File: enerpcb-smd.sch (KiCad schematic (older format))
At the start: 22 parts, among them K1 VS1, K2 VS2, K3 CONN_1, K4 CONN_1, P2 IO1, P3 IO2, P4 PROGRAM, P5 V1, P6 V2, P7 GND1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

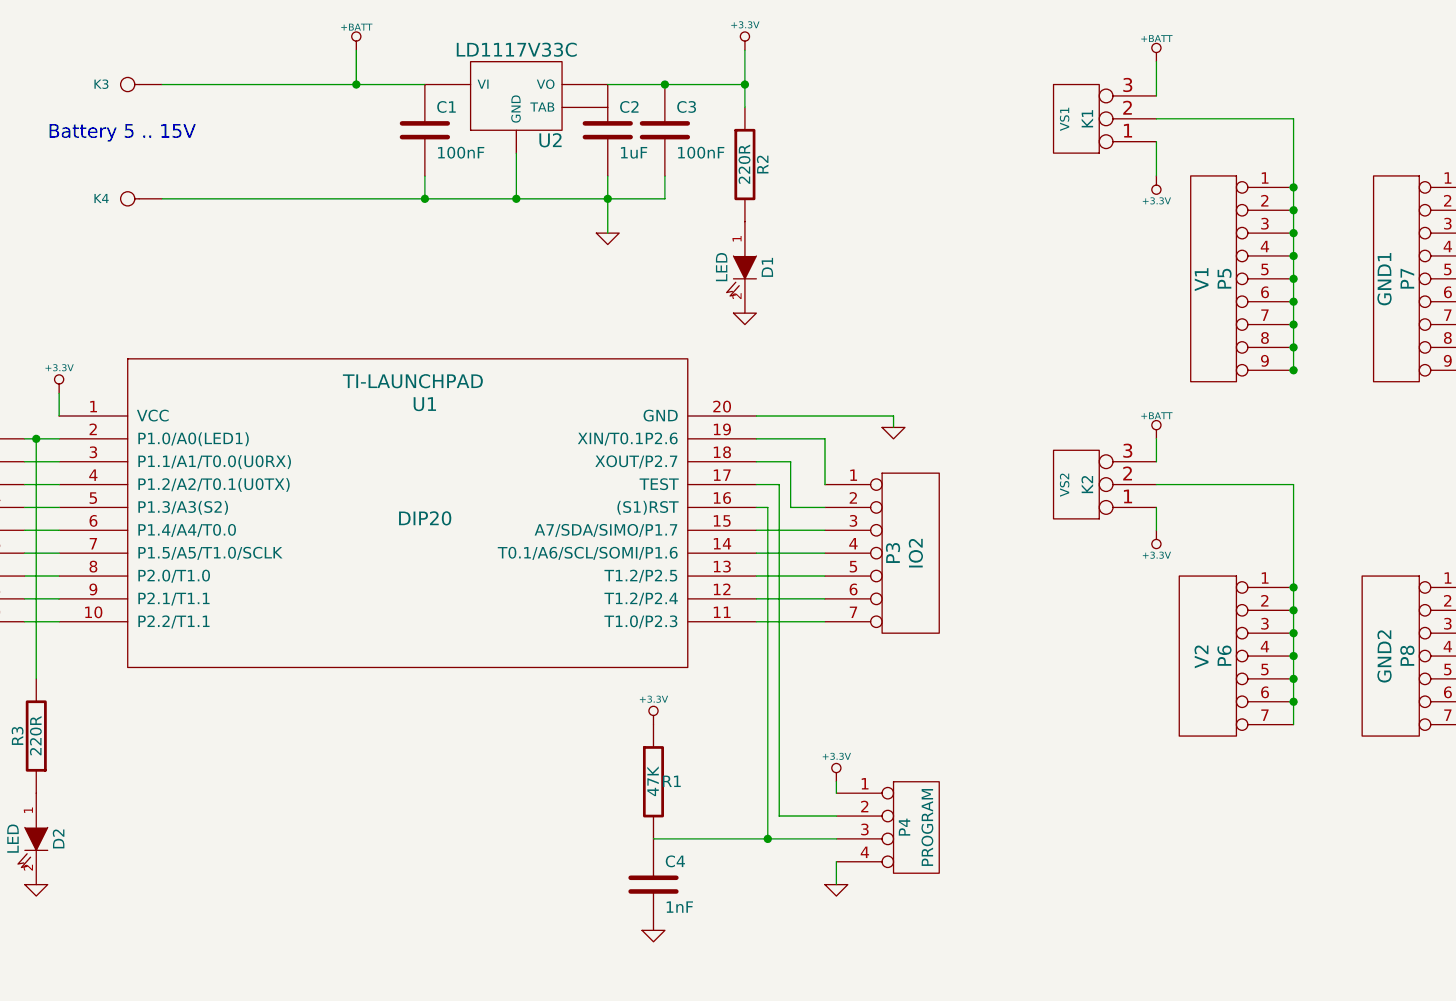
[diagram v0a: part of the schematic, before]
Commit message: Routed SMD version: OK
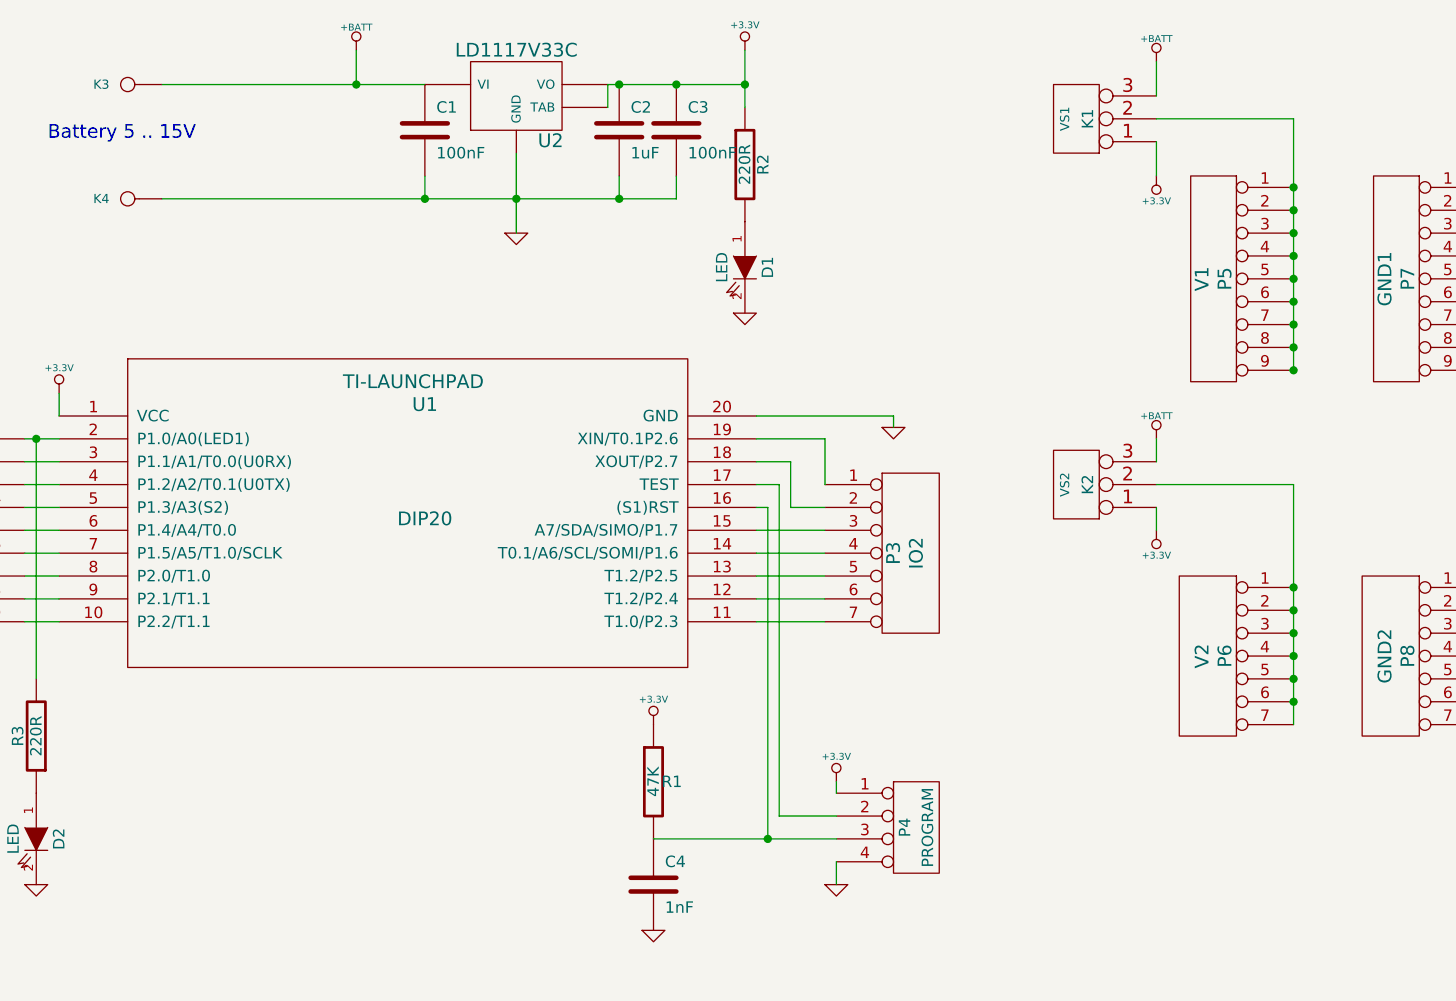
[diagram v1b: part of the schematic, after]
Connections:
- net +3.3V: now also U2.4 (TAB)
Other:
- moved on the sheet: C2, C3
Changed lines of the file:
@@
-EESchema Schematic File Version 2  date 1/1/2013 8:38:13 PM
+EESchema Schematic File Version 2  date 1/5/2013 4:17:03 PM
 LIBS:power
 LIBS:device
@@
 LIBS:valves
 LIBS:ti-launchpad
-LIBS:enerpcb-cache
+LIBS:enerpcb-smd-cache
 EELAYER 25  0
 EELAYER END
@@
 Sheet 1 1
 Title ""
-Date "1 jan 2013"
+Date "5 jan 2013"
 Rev ""
 Comp ""
@@
 $EndDescr
 Wire Wire Line
-	7000 2250 7000 1150
-Wire Wire Line
-	5250 2500 5250 2450
-Wire Wire Line
-	5250 2450 4650 2450
-Wire Wire Line
-	4950 2750 4950 2550
-Wire Wire Line
-	4950 2550 4650 2550
-Wire Wire Line
-	4650 2750 4750 2750
+	2050 1500 4300 1500
+Wire Wire Line
+	4600 1000 4000 1000
+Wire Wire Line
+	4000 1000 4000 1100
+Wire Wire Line
+	4800 2850 4800 2650
+Wire Wire Line
+	4800 2850 4950 2850
+Wire Wire Line
+	4650 2850 4700 2850
+Wire Wire Line
+	4950 2950 4650 2950
+Wire Wire Line
+	4950 3150 4650 3150
+Wire Wire Line
+	4950 3350 4650 3350
+Wire Wire Line
+	4750 4200 4750 2750
+Connection ~ 1500 2550
+Wire Wire Line
+	1500 2550 1500 3600
+Wire Wire Line
+	1450 3250 1600 3250
+Wire Wire Line
+	1450 3050 1600 3050
+Wire Wire Line
+	1450 2850 1600 2850
+Wire Wire Line
+	1450 2650 1600 2650
+Wire Wire Line
+	5000 4300 4200 4300
+Wire Wire Line
+	5000 4400 5000 4500
+Connection ~ 4600 1000
+Wire Wire Line
+	4600 850  4600 1100
+Wire Wire Line
+	2050 1000 3200 1000
+Connection ~ 3200 1500
+Wire Wire Line
+	3200 1500 3200 1400
+Wire Wire Line
+	7800 1450 7800 4000
+Wire Wire Line
+	7000 3800 7000 2750
+Wire Wire Line
+	7000 2750 6400 2750
+Wire Wire Line
+	6400 2550 6400 2650
+Connection ~ 7800 3800
+Connection ~ 7800 3600
+Connection ~ 7800 3400
+Connection ~ 7800 3300
+Connection ~ 7800 2250
+Connection ~ 7800 2050
+Connection ~ 7800 1950
+Connection ~ 7800 1750
+Connection ~ 7800 1550
+Connection ~ 7000 3700
+Connection ~ 7000 3500
+Connection ~ 7000 3200
+Connection ~ 7000 2150
+Connection ~ 7000 1950
+Connection ~ 7000 1750
+Connection ~ 7000 1550
+Wire Wire Line
+	6400 1150 7000 1150
+Wire Wire Line
+	6400 900  6400 1050
+Wire Wire Line
+	1600 2350 1600 2450
+Wire Wire Line
+	2900 850  2900 1000
+Connection ~ 2900 1000
+Wire Wire Line
+	6400 1400 6400 1250
+Connection ~ 7000 1450
+Connection ~ 7000 1650
+Connection ~ 7000 1850
+Connection ~ 7000 2050
+Connection ~ 7000 2250
+Connection ~ 7000 3400
+Connection ~ 7000 3300
+Connection ~ 7000 3600
+Connection ~ 7800 1650
+Connection ~ 7800 1850
+Connection ~ 7800 2150
+Connection ~ 7800 3200
+Connection ~ 7800 3500
+Connection ~ 7800 3700
+Wire Wire Line
+	6400 2850 6400 2950
+Connection ~ 3600 1500
+Wire Wire Line
+	4300 1500 4300 1400
+Connection ~ 4300 1000
+Wire Wire Line
+	5000 4100 5000 4050
+Wire Wire Line
+	1450 2550 1600 2550
+Wire Wire Line
+	1450 2750 1600 2750
+Wire Wire Line
+	1450 2950 1600 2950
+Wire Wire Line
+	1450 3150 1600 3150
+Wire Wire Line
+	1450 3350 1600 3350
+Wire Wire Line
+	4800 2650 4650 2650
+Wire Wire Line
+	4750 4200 5000 4200
+Wire Wire Line
+	4700 2850 4700 4300
+Connection ~ 4700 4300
+Wire Wire Line
+	4950 3250 4650 3250
 Wire Wire Line
 	4950 3050 4650 3050
 Wire Wire Line
-	4950 3250 4650 3250
-Connection ~ 4700 4300
-Wire Wire Line
-	4700 4300 4700 2850
-Wire Wire Line
-	5000 4200 4750 4200
-Wire Wire Line
-	4650 2650 4800 2650
-Wire Wire Line
-	1450 3350 1600 3350
-Wire Wire Line
-	1450 3150 1600 3150
-Wire Wire Line
-	1450 2950 1600 2950
-Wire Wire Line
-	1450 2750 1600 2750
-Wire Wire Line
-	1450 2550 1600 2550
-Wire Wire Line
-	5000 4100 5000 4050
-Connection ~ 4250 1000
-Wire Wire Line
-	4250 1400 4250 1500
-Wire Wire Line
-	4250 1500 2050 1500
-Connection ~ 3600 1500
-Wire Wire Line
-	3600 1500 3600 1300
-Wire Wire Line
-	6400 2850 6400 2950
-Connection ~ 7800 3700
-Connection ~ 7800 3500
-Connection ~ 7800 3200
-Connection ~ 7800 2150
-Connection ~ 7800 1850
-Connection ~ 7800 1650
-Connection ~ 7000 3600
-Connection ~ 7000 3300
-Connection ~ 7000 3400
-Connection ~ 7000 2250
-Connection ~ 7000 2050
-Connection ~ 7000 1850
-Connection ~ 7000 1650
-Connection ~ 7000 1450
-Wire Wire Line
-	6400 1400 6400 1250
-Connection ~ 2900 1000
-Wire Wire Line
-	2900 850  2900 1000
-Wire Wire Line
-	1600 2350 1600 2450
-Wire Wire Line
-	6400 900  6400 1050
-Wire Wire Line
-	7000 1150 6400 1150
-Connection ~ 7000 1550
-Connection ~ 7000 1750
-Connection ~ 7000 1950
-Connection ~ 7000 2150
-Connection ~ 7000 3200
-Connection ~ 7000 3500
-Connection ~ 7000 3700
-Connection ~ 7800 1550
-Connection ~ 7800 1750
-Connection ~ 7800 1950
-Connection ~ 7800 2050
-Connection ~ 7800 2250
-Connection ~ 7800 3300
-Connection ~ 7800 3400
-Connection ~ 7800 3600
-Connection ~ 7800 3800
-Wire Wire Line
-	6400 2550 6400 2650
-Wire Wire Line
-	6400 2750 7000 2750
-Wire Wire Line
-	7000 2750 7000 3800
-Wire Wire Line
-	7800 1450 7800 4000
-Wire Wire Line
-	3200 1500 3200 1400
-Connection ~ 3200 1500
-Connection ~ 4000 1500
-Wire Wire Line
-	4000 1650 4000 1400
-Wire Wire Line
-	2050 1000 3200 1000
-Wire Wire Line
-	4600 1000 4000 1000
-Wire Wire Line
-	4600 850  4600 1100
-Connection ~ 4600 1000
-Wire Wire Line
-	5000 4400 5000 4500
-Wire Wire Line
-	5000 4300 4200 4300
-Wire Wire Line
-	1450 2650 1600 2650
-Wire Wire Line
-	1450 2850 1600 2850
-Wire Wire Line
-	1450 3050 1600 3050
-Wire Wire Line
-	1450 3250 1600 3250
-Wire Wire Line
-	1500 2550 1500 3600
-Connection ~ 1500 2550
-Wire Wire Line
-	4750 4200 4750 2750
-Wire Wire Line
-	4950 3350 4650 3350
-Wire Wire Line
-	4950 3150 4650 3150
-Wire Wire Line
-	4950 2950 4650 2950
-Wire Wire Line
-	4700 2850 4650 2850
-Wire Wire Line
-	4950 2850 4800 2850
-Wire Wire Line
-	4800 2850 4800 2650
+	4750 2750 4650 2750
+Wire Wire Line
+	4650 2550 4950 2550
+Wire Wire Line
+	4950 2550 4950 2750
+Wire Wire Line
+	4650 2450 5250 2450
+Wire Wire Line
+	5250 2450 5250 2500
+Wire Wire Line
+	7000 1150 7000 2250
+Wire Wire Line
+	3600 1650 3600 1300
+Connection ~ 4050 1000
+Wire Wire Line
+	4050 1400 4050 1500
+Connection ~ 4050 1500
+$Comp
+L LD1117V33C U2
+U 1 1 50E2C9E5
+P 3600 1050
+F 0 "U2" H 3750 854 60  0000 C CNN
+F 1 "LD1117V33C" H 3600 1250 60  0000 C CNN
+	1    3600 1050
+	1    0    0    -1
+$EndComp
 Text Notes 1550 1250 0    60   ~ 0
 Battery 5 .. 15V
@@
 $EndComp
 $Comp
-L LD1117V33C U2
-U 1 1 50E2C9E5
-P 3600 1050
-F 0 "U2" H 3750 854 60  0000 C CNN
-F 1 "LD1117V33C" H 3600 1250 60  0000 C CNN
-	1    3600 1050
-	1    0    0    -1
-$EndComp
-$Comp
 L GND #PWR02
 U 1 1 50E2C789
@@
 L C C3
 U 1 1 50E2C4B7
-P 4250 1200
-F 0 "C3" H 4300 1300 50  0000 L CNN
-F 1 "100nF" H 4300 1100 50  0000 L CNN
-	1    4250 1200
+P 4300 1200
+F 0 "C3" H 4350 1300 50  0000 L CNN
+F 1 "100nF" H 4350 1100 50  0000 L CNN
+	1    4300 1200
 	1    0    0    -1
 $EndComp
@@
 L GND #PWR04
 U 1 1 50E1B581
-P 4000 1650
-F 0 "#PWR04" H 4000 1650 30  0001 C CNN
-F 1 "GND" H 4000 1580 30  0001 C CNN
-	1    4000 1650
+P 3600 1650
+F 0 "#PWR04" H 3600 1650 30  0001 C CNN
+F 1 "GND" H 3600 1580 30  0001 C CNN
+	1    3600 1650
 	1    0    0    -1
 $EndComp
@@
 L C C2
 U 1 1 50E1969F
-P 4000 1200
-F 0 "C2" H 4050 1300 50  0000 L CNN
-F 1 "1uF" H 4050 1100 50  0000 L CNN
-	1    4000 1200
-	1    0    0    -1
-$EndComp
+P 4050 1200
+F 0 "C2" H 4100 1300 50  0000 L CNN
+F 1 "1uF" H 4100 1100 50  0000 L CNN
+	1    4050 1200
+	1    0    0    -1
+$EndComp

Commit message: As ordered
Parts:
- C1, C3: Farnell (none) -> 1856307; PRICE (none) -> 0.06
- C2: Farnell (none) -> 1856632; PRICE (none) -> 0.06
- C4: Farnell (none) -> 1856408; PRICE (none) -> 0.06
- D1: value LED -> LED-R; footprint (none) -> LED0603; Farnell (none) -> 8554641; MFG (none) -> HSMH-C190; PRICE (none) -> 0.06
- D2: value LED -> LED-G; footprint (none) -> LED0603; Farnell (none) -> 1226372; MFG (none) -> LGQ971; PRICE (none) -> 0.07
- P2: Farnell (none) -> 2035689; MFG (none) -> SAMTEC TSW-109-07-T-S; PRICE (none) -> 0.85
- P3: Farnell (none) -> 1924186; MFG (none) -> FCI 68000-107HLF; PRICE (none) -> 0.42
- P4: footprint (none) -> SIL-4; Farnell (none) -> 1756958; MFG (none) -> MOLEX 90120-0124 HEADER, 2.54MM, 4WAY; PRICE (none) -> 0.15
- P5, P7: Farnell (none) -> 2035689; PRICE (none) -> 0.85
- P6, P8: Farnell (none) -> 1924186; PRICE (none) -> 0.42
- R1: Farnell (none) -> 2074475; PRICE (none) -> 0.03
- R2, R3: Farnell (none) -> 9233920; PRICE (none) -> 0.03
- U1: value TI-LAUNCHPAD -> MSP430G2212IPW20; footprint DIP20 -> TSSOP20; Farnell (none) -> 1866866; MFG (none) -> TI MSP430G2212IPW20 2kB FLASH 256b RAM; PRICE (none) -> 0.7
- U2: Farnell (none) -> 1467776; PRICE (none) -> 1
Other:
- note added: "MSP430G2212IPW20: FARNELL# 1866866 (2kB 256b 1xTA3 8xCMP), E0.70@1, E0.56@100"
- note added: "MSP430G2302IPW20: FARNELL# 1866883 (4kB 256b 1xTA3 8xCMP), E1.6@1, E0.68@100"
- note added: "MSP430G2352IPW20: FARNELL# 1866896 (4kB 256b 1xTA3 8xCMP 8xADC), E0.90@1, E0.69@100"
- note added: "MSP430G2452IPW20R: FARNELL# 1865387 (8kB 256b 1xTA3 8xCMP, 8xADC), E2.48@1, E0.80@100"
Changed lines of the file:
@@
-EESchema Schematic File Version 2  date 1/5/2013 4:17:03 PM
+EESchema Schematic File Version 2  date 1/6/2013 1:15:40 AM
 LIBS:power
 LIBS:device
@@
 Sheet 1 1
 Title ""
-Date "5 jan 2013"
+Date "6 jan 2013"
 Rev ""
 Comp ""
@@
 Comment4 ""
 $EndDescr
+Text Notes 1300 5550 0    100  ~ 0
+MSP430G2452IPW20R: FARNELL#  1865387  (8kB 256b 1xTA3 8xCMP, 8xADC), E2.48@1, E0.80@100
+Text Notes 1300 5150 0    100  ~ 0
+MSP430G2302IPW20: FARNELL#  1866883  (4kB 256b 1xTA3 8xCMP), E1.6@1, E0.68@100
+Text Notes 1300 4950 0    100  ~ 0
+MSP430G2212IPW20: FARNELL#  1866866 (2kB 256b 1xTA3 8xCMP), E0.70@1, E0.56@100
+Text Notes 1300 5350 0    100  ~ 0
+MSP430G2352IPW20: FARNELL#  1866896 (4kB 256b 1xTA3 8xCMP 8xADC), E0.90@1, E0.69@100
 Wire Wire Line
 	2050 1500 4300 1500
@@
 F 0 "U2" H 3750 854 60  0000 C CNN
 F 1 "LD1117V33C" H 3600 1250 60  0000 C CNN
+F 4 "1467776 " H 3600 1050 60  0001 C CNN "Farnell"
+F 5 "1" H 3600 1050 60  0001 C CNN "PRICE"
 	1    3600 1050
 	1    0    0    -1
@@
 P 1500 4300
 F 0 "D2" H 1500 4400 50  0000 C CNN
-F 1 "LED" H 1500 4200 50  0000 C CNN
+F 1 "LED-G" H 1500 4200 50  0000 C CNN
+F 2 "LED0603" H 1500 4300 60  0001 C CNN
+F 4 "1226372 " H 1500 4300 60  0001 C CNN "Farnell"
+F 5 "0.07" H 1500 4300 60  0001 C CNN "PRICE"
+F 6 "LGQ971 " H 1500 4300 60  0001 C CNN "MFG"
 	1    1500 4300
 	0    1    1    0
@@
 F 0 "R3" V 1580 3850 50  0000 C CNN
 F 1 "220R" V 1500 3850 50  0000 C CNN
+F 4 " 9233920" H 1500 3850 60  0001 C CNN "Farnell"
+F 5 "0.03" H 1500 3850 60  0001 C CNN "PRICE"
 	1    1500 3850
 	-1   0    0    1
@@
 F 0 "C3" H 4350 1300 50  0000 L CNN
 F 1 "100nF" H 4350 1100 50  0000 L CNN
+F 4 "1856307" H 4300 1200 60  0001 C CNN "Farnell"
+F 5 "0.06" H 4300 1200 60  0001 C CNN "PRICE"
 	1    4300 1200
 	1    0    0    -1
@@
 F 0 "C4" H 4250 4600 50  0000 L CNN
 F 1 "1nF" H 4250 4400 50  0000 L CNN
+F 4 "1856408" H 4200 4500 60  0001 C CNN "Farnell"
+F 5 "0.06" H 4200 4500 60  0001 C CNN "PRICE"
 	1    4200 4500
 	1    0    0    -1
@@
 F 0 "R2" V 4680 1350 50  0000 C CNN
 F 1 "220R" V 4600 1350 50  0000 C CNN
+F 4 " 9233920" H 4600 1350 60  0001 C CNN "Farnell"
+F 5 "0.03" H 4600 1350 60  0001 C CNN "PRICE"
 	1    4600 1350
 	1    0    0    -1
@@
 P 4600 1800
 F 0 "D1" H 4600 1900 50  0000 C CNN
-F 1 "LED" H 4600 1700 50  0000 C CNN
+F 1 "LED-R" H 4600 1700 50  0000 C CNN
+F 2 "LED0603" H 4600 1800 60  0001 C CNN
+F 4 "8554641" H 4600 1800 60  0001 C CNN "Farnell"
+F 5 "0.06" H 4600 1800 60  0001 C CNN "PRICE"
+F 6 "HSMH-C190" H 4600 1800 60  0001 C CNN "MFG"
 	1    4600 1800
 	0    1    1    0
@@
 F 0 "R1" H 4280 4050 50  0000 C CNN
 F 1 "47K" V 4200 4050 50  0000 C CNN
+F 4 "2074475 " H 4200 4050 60  0001 C CNN "Farnell"
+F 5 "0.03" H 4200 4050 60  0001 C CNN "PRICE"
 	1    4200 4050
 	1    0    0    -1
@@
 F 0 "P8" V 7400 3500 60  0000 C CNN
 F 1 "GND2" V 7500 3500 60  0000 C CNN
+F 4 "1924186" H 7450 3500 60  0001 C CNN "Farnell"
+F 5 "0.42" H 7450 3500 60  0001 C CNN "PRICE"
 	1    7450 3500
 	-1   0    0    -1
@@
 F 0 "P7" V 7400 1850 60  0000 C CNN
 F 1 "GND1" V 7500 1850 60  0000 C CNN
+F 4 "2035689 " H 7450 1850 60  0001 C CNN "Farnell"
+F 5 "0.85" H 7450 1850 60  0001 C CNN "PRICE"
 	1    7450 1850
 	-1   0    0    -1
@@
 F 0 "C2" H 4100 1300 50  0000 L CNN
 F 1 "1uF" H 4100 1100 50  0000 L CNN
+F 4 "1856632 " H 4050 1200 60  0001 C CNN "Farnell"
+F 5 "0.06" H 4050 1200 60  0001 C CNN "PRICE"
 	1    4050 1200
 	1    0    0    -1
@@
 F 0 "C1" H 3250 1300 50  0000 L CNN
 F 1 "100nF" H 3250 1100 50  0000 L CNN
+F 4 "1856307" H 3200 1200 60  0001 C CNN "Farnell"
+F 5 "0.06" H 3200 1200 60  0001 C CNN "PRICE"
 	1    3200 1200
 	1    0    0    -1
@@
 F 0 "P6" V 6600 3500 60  0000 C CNN
 F 1 "V2" V 6700 3500 60  0000 C CNN
+F 4 "1924186" H 6650 3500 60  0001 C CNN "Farnell"
+F 5 "0.42" H 6650 3500 60  0001 C CNN "PRICE"
 	1    6650 3500
 	-1   0    0    -1
@@
 F 0 "P5" V 6600 1850 60  0000 C CNN
 F 1 "V1" V 6700 1850 60  0000 C CNN
+F 4 "2035689 " H 6650 1850 60  0001 C CNN "Farnell"
+F 5 "0.85" H 6650 1850 60  0001 C CNN "PRICE"
 	1    6650 1850
 	-1   0    0    -1
@@
 F 0 "P4" V 5300 4250 50  0000 C CNN
 F 1 "PROGRAM" V 5400 4250 50  0000 C CNN
+F 2 "SIL-4" H 5350 4250 60  0001 C CNN
+F 4 "1756958" H 5350 4250 60  0001 C CNN "Farnell"
+F 5 "0.15" H 5350 4250 60  0001 C CNN "PRICE"
+F 6 "MOLEX 90120-0124  HEADER, 2.54MM, 4WAY" H 5350 4250 60  0001 C CNN "MFG"
 	1    5350 4250
 	1    0    0    -1
@@
 F 0 "P2" V 1050 2950 60  0000 C CNN
 F 1 "IO1" V 1150 2950 60  0000 C CNN
+F 4 "2035689 " H 1100 2950 60  0001 C CNN "Farnell"
+F 5 "0.85" H 1100 2950 60  0001 C CNN "PRICE"
+F 6 "SAMTEC TSW-109-07-T-S " H 1100 2950 60  0001 C CNN "MFG"
 	1    1100 2950
 	-1   0    0    -1
@@
 F 0 "P3" V 5250 3050 60  0000 C CNN
 F 1 "IO2" V 5350 3050 60  0000 C CNN
+F 4 "1924186" H 5300 3050 60  0001 C CNN "Farnell"
+F 5 "0.42" H 5300 3050 60  0001 C CNN "PRICE"
+F 6 "FCI 68000-107HLF " H 5300 3050 60  0001 C CNN "MFG"
 	1    5300 3050
 	1    0    0    -1
@@
 P 3200 2900
 F 0 "U1" H 3200 3400 60  0000 C CNN
-F 1 "TI-LAUNCHPAD" H 3150 3500 60  0000 C CNN
-F 2 "DIP20" H 3200 2900 60  0000 C CNN
+F 1 "MSP430G2212IPW20 " H 3150 3500 60  0000 C CNN
+F 2 "TSSOP20" H 3200 2900 60  0000 C CNN
+F 4 " 1866866 " H 3200 2900 60  0001 C CNN "Farnell"
+F 5 "0.7" H 3200 2900 60  0001 C CNN "PRICE"
+F 6 "TI MSP430G2212IPW20 2kB FLASH 256b RAM" H 3200 2900 60  0001 C CNN "MFG"
 	1    3200 2900
 	1    0    0    -1
